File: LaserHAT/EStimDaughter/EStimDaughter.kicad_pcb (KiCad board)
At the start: 4 copper layers, 26.5 x 36.5 mm, 53 parts, among them J1 ELECTRODE E1/E2, J8 J8 power/timing (underside), J9 J9 I2C/release (underside), U1 ISO7741FDBQR, U2 TLV76050DBZR, U4 DAC60501ZDGSR, U5 OPA2192IDGKR, U6 74HC4053BQ, U7 DG419BDQ, U8 TLV1702AIDGKR, U9 ISO1640BDR

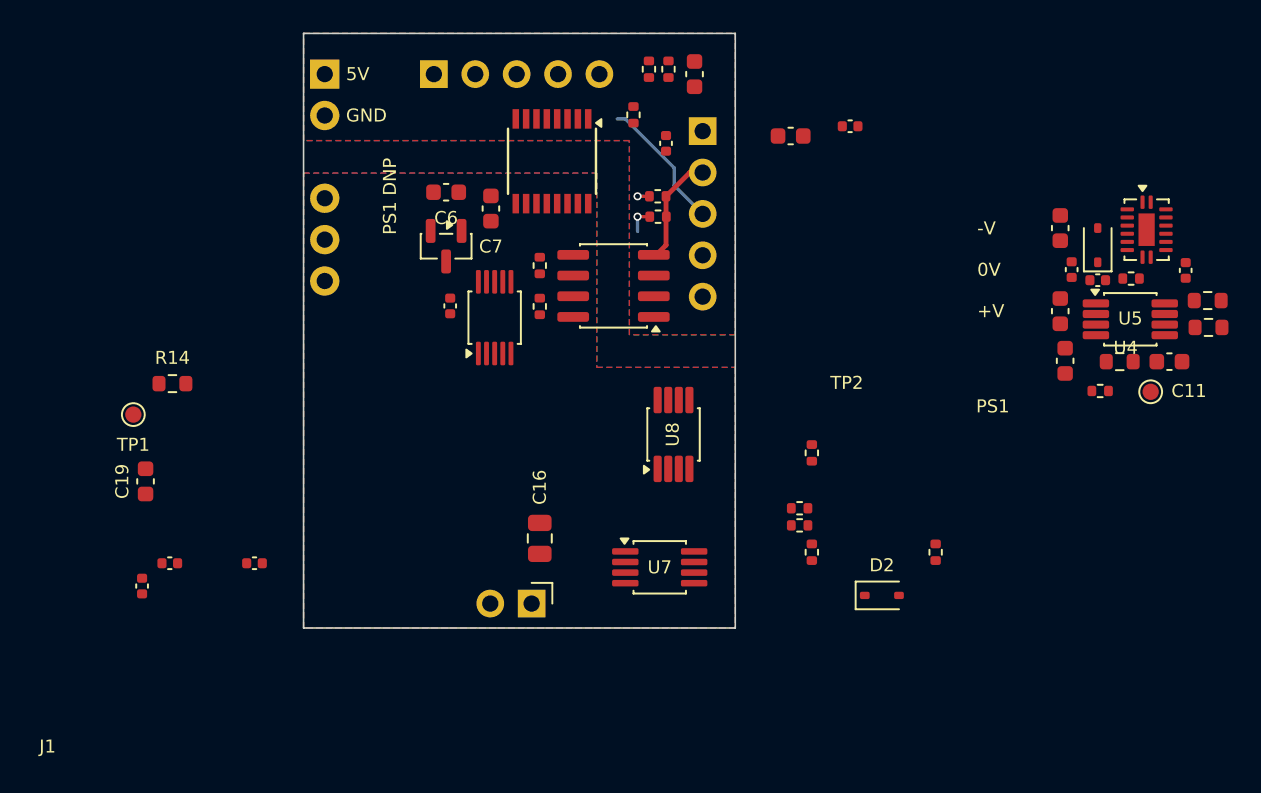
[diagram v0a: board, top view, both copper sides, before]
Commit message: EStimDaughter M4c: ADG1436 switch, U8 units swapped, J8.3/J8.5 = FAULT/EN, 4-layer routed with In2 rail pours
Circuit
- 74HC4053 + the -5 V zener rail (R6, D1, C8) -> one ADG1436YCPZ (LFCSP-16 4x4, +/-15 V dual SPDT):
  switch 1 (IN1 = EN) gates 0 V / SW_P -> V_IN, switch 2 (IN2 = CATH) picks VSET_P / VSET_N -> SW_P;
  EN pin on VDD (+V_STIM). C13/C14 are 100 n 50 V +/-V taps; C4 and C20 dropped, C2 serves both
  isolator VCC2 pins. -V rail load now ~1.5 mA: below the Mornsun A0515S minimum, RECOM RB-0515D/HP
  or batteries are unaffected.
- U8 comparator halves swapped (B = TH_P edge). U1 channels A/B/C = RELEASE/EN/CATH.
- Connector standard: J8.3 = FAULT_n (PA6, TIMA0_FAULT0), J8.5 = EN (PA7); J9.4 = SDA, J9.5 = SCL.
  HAT copper and the laser module must follow: spec section 3/7 and LAYOUT_HANDOFF open questions.

Schematic generator
- Deterministic UUIDs (uuid5 of the reference); footprints carry KiCad's root-sheet paths, full
  Lib:Name FPIDs and the schematic's net names, so F8 is a no-op. VSET_P / VSET_N labelled.

Board
- Outline y 76-109. 4 layers: F parts/signals + GND pours, In1 split GND planes, In2 power
  (user-routed 0.8 mm traces plus generated per-rail pours shaped by that routing), B logic runs.
- Decoupling moved onto pins (C10 at U4, C11/C12 at U5/U7, C2 between U1/U9); labels back on
  board; DRC: 0 unconnected, 0 electrical errors, schematic parity clean.

Co-Authored-By: Claude Fable 5.1 <noreply@anthropic.com>
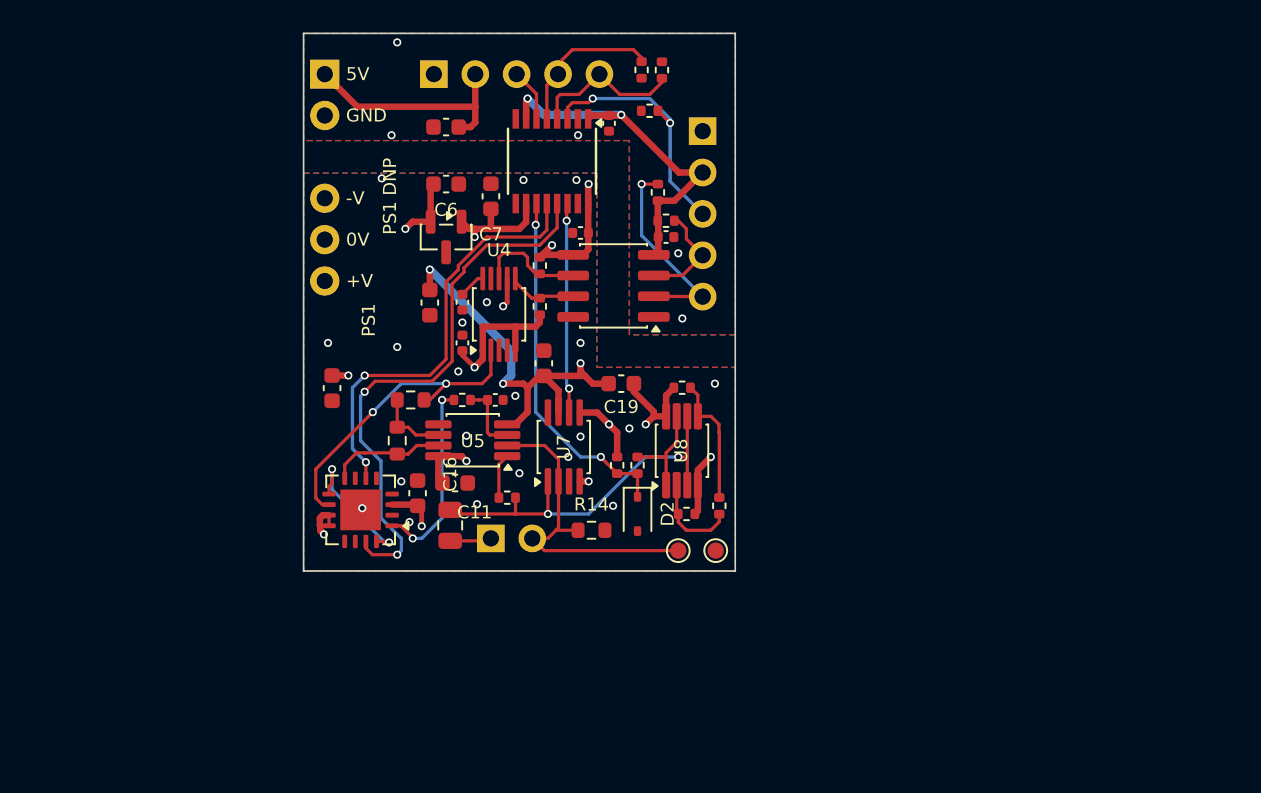
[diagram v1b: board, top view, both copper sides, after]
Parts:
- removed C20: 100n, C_0402_1005Metric
- removed C4, C8: 1u 50V, C_0603_1608Metric
- removed D1: BZT52C4V7S, D_SOD-323
- removed R6: 1.5k, R_0603_1608Metric
- C1, C10, C15, C17, C2, C9: footprint C_0402_1005Metric -> Capacitor_SMD:C_0402_1005Metric
- C11, C12, C3, C5, C6, C7: footprint C_0603_1608Metric -> Capacitor_SMD:C_0603_1608Metric
- C13, C14: footprint C_0402_1005Metric -> Capacitor_SMD:C_0603_1608Metric
- C16: footprint C_0805_2012Metric -> Capacitor_SMD:C_0805_2012Metric
- J1: footprint PinHeader_1x02_P2.54mm_Horizontal -> Connector_PinHeader_2.54mm:PinHeader_1x02_P2.54mm_Horizontal; moved to B.Cu
- J8, J9: footprint PinHeader_1x05_P2.54mm_Vertical -> Connector_PinHeader_2.54mm:PinHeader_1x05_P2.54mm_Vertical
- PS1: footprint DCDC_SIP6_A0515S -> estim:DCDC_SIP6_A0515S
- R1, R12, R13, R15, R19, R2, R23, R24, R25, R26, R3, R7, R8, R9: footprint R_0402_1005Metric -> Resistor_SMD:R_0402_1005Metric
- R10, R11, R14: footprint R_0603_1608Metric -> Resistor_SMD:R_0603_1608Metric
- TP1, TP2: footprint TestPoint_Pad_D1.0mm -> TestPoint:TestPoint_Pad_D1.0mm
- U1: footprint SSOP-16_3.9x4.9mm_P0.635mm -> Package_SO:SSOP-16_3.9x4.9mm_P0.635mm
- U2: footprint SOT-23 -> Package_TO_SOT_SMD:SOT-23
- U4: footprint VSSOP-10_3x3mm_P0.5mm -> Package_SO:VSSOP-10_3x3mm_P0.5mm
- U5, U8: footprint VSSOP-8_3x3mm_P0.65mm -> Package_SO:VSSOP-8_3x3mm_P0.65mm
- U6: value 74HC4053BQ -> ADG1436YCPZ; footprint DHVQFN-16-1EP_2.5x3.5mm_P0.5mm_EP1x2mm -> Package_DFN_QFN:QFN-16-1EP_4x4mm_P0.65mm_EP2.5x2.5mm
- U7: footprint MSOP-8_3x3mm_P0.65mm -> Package_SO:MSOP-8_3x3mm_P0.65mm
- U9: footprint SOIC-8_3.9x4.9mm_P1.27mm -> Package_SO:SOIC-8_3.9x4.9mm_P1.27mm
- moved U6 51.2 mm to (104.5, 105.2), turned to 180 degrees
- moved R11 50.3 mm to (106.8, 101.0), turned to -90 degrees
- moved R10 49.3 mm to (107.6, 98.5), turned to 180 degrees
- moved C10 44.6 mm to (110.8, 95.0)
- moved C11 44.5 mm to (110.3, 103.6)
- moved C14 42.4 mm to (108.0, 104.2), turned to -90 degrees
- moved R12 41.7 mm to (110.7, 98.5)
- moved U5 41.0 mm to (111.4, 101.0), turned to 180 degrees
- moved C5 39.0 mm to (108.8, 92.5)
- moved C15 37.7 mm to (112.8, 98.5)
- moved R13 37.0 mm to (113.5, 104.5)
- moved C13 35.6 mm to (102.8, 97.8), turned to -90 degrees
- moved C1 34.7 mm to (119.8, 81.5), turned to -90 degrees
- moved TP1 34.5 mm to (124.0, 107.8)
- moved C2 32.4 mm to (118.0, 88.2), turned to 180 degrees
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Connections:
- net RELEASE_H renamed /RELEASE_H
- net SCL_H renamed /SCL_H
- net SDA_H renamed /SDA_H
- C13 pad 1: +5V_ISO -> +V_STIM
- C14 pad 2: -5V_ISO -> -V_STIM
- J8 pad 3: EN_H -> /FAULT_H
- J8 pad 4: CATH_H -> /CATH_H
- J8 pad 5: FAULT_H -> /EN_H
- R1 pad 1: EN_H -> /EN_H
- R10 pad 1: Net-(U4-VOUT) -> /VSET_P
- R11 pad 2: Net-(U6-1Y1) -> /VSET_N
- R2 pad 1: CATH_H -> /CATH_H
- R23 pad 2: Net-(U8A-+) -> Net-(U8B-+)
- R24 pad 1: Net-(U8A-+) -> Net-(U8B-+)
- R24 pad 2: Net-(U8B--) -> Net-(U8A--)
- R25 pad 1: Net-(U8B--) -> Net-(U8A--)
- U1 pad 12: EN -> CATH
- U1 pad 13: CATH -> EN
- U1 pad 4: CATH_H -> /EN_H
- U1 pad 5: EN_H -> /CATH_H
- U1 pad 6: FAULT_H -> /FAULT_H
- U4 pad 2: Net-(U4-VOUT) -> /VSET_P
- U5 pad 7: Net-(U6-1Y1) -> /VSET_N
- U6 pad 1: SW_P -> V_IN
- U6 pad 10: EN -> /VSET_P
- U6 pad 11: CATH -> +V_STIM
- U6 pad 12: Net-(U4-VOUT) -> +V_STIM
- U6 pad 13: Net-(U6-1Y1) -> unconnected-(U6-NC-Pad13)
- U6 pad 14: SW_P -> unconnected-(U6-NC-Pad14)
- U6 pad 15: V_IN -> EN
- U6 pad 16: +5V_ISO -> /SW_P
- U6 pad 17: (no net) -> -V_STIM
- U6 pad 3: GND_ISO -> -V_STIM
- U6 pad 5: GND_ISO -> unconnected-(U6-NC-Pad5)
- U6 pad 6: GND_ISO -> CATH
- U6 pad 7: -5V_ISO -> unconnected-(U6-NC-Pad7)
- U6 pad 8: GND_ISO -> /VSET_N
- U6 pad 9: GND_ISO -> /SW_P
- U8 pad 2: E1 -> Net-(U8A--)
- U8 pad 3: Net-(U8A-+) -> E1
- U8 pad 5: E1 -> Net-(U8B-+)
- U8 pad 6: Net-(U8B--) -> E1
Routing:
- net -V_STIM: track 0.00 -> 79.2 mm, vias 0 -> 6
- net +V_STIM: track 0.00 -> 67.2 mm, vias 0 -> 6
- net +5V_ISO: track 0.00 -> 57.9 mm, vias 0 -> 5
- net EN: track 0.00 -> 34.1 mm, vias 0 -> 2
- net CATH: track 0.00 -> 26.4 mm, vias 0 -> 2
- net E1: track 0.00 -> 23.3 mm, vias 0 -> 2
- net FAULT_n: track 0.00 -> 22.1 mm, vias 0 -> 2
- net ISENSE: track 0.00 -> 20.2 mm
- net /VSET_P: track 0.00 -> 19.2 mm, vias 0 -> 2
- net +3V3_H: track 6.85 -> 23.1 mm, vias 0 -> 2
- net +5V_H: track 0.00 -> 14.2 mm
- net RELEASE: track 0.00 -> 12.3 mm, vias 0 -> 2
- net V_IN: track 0.00 -> 11.9 mm, vias 0 -> 2
- net /SCL_H: track 1.75 -> 13.1 mm
- net /CATH_H: track 0.00 -> 9.59 mm
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- added copper zone on In2.Cu, net +5V_ISO
- added copper zone on In2.Cu, net +V_STIM
- added copper zone on In2.Cu, net -V_STIM
- removed copper zone on In2.Cu, net GND_H
- removed copper zone on In2.Cu, net GND_ISO
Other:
- board size 26.5 x 36.5 mm -> 26.5 x 33 mm
